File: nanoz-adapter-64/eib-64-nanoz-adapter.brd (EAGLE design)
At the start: 24 x 63.5 mm, 4 parts, among them J1 DF40-REC, J4 SCREW2

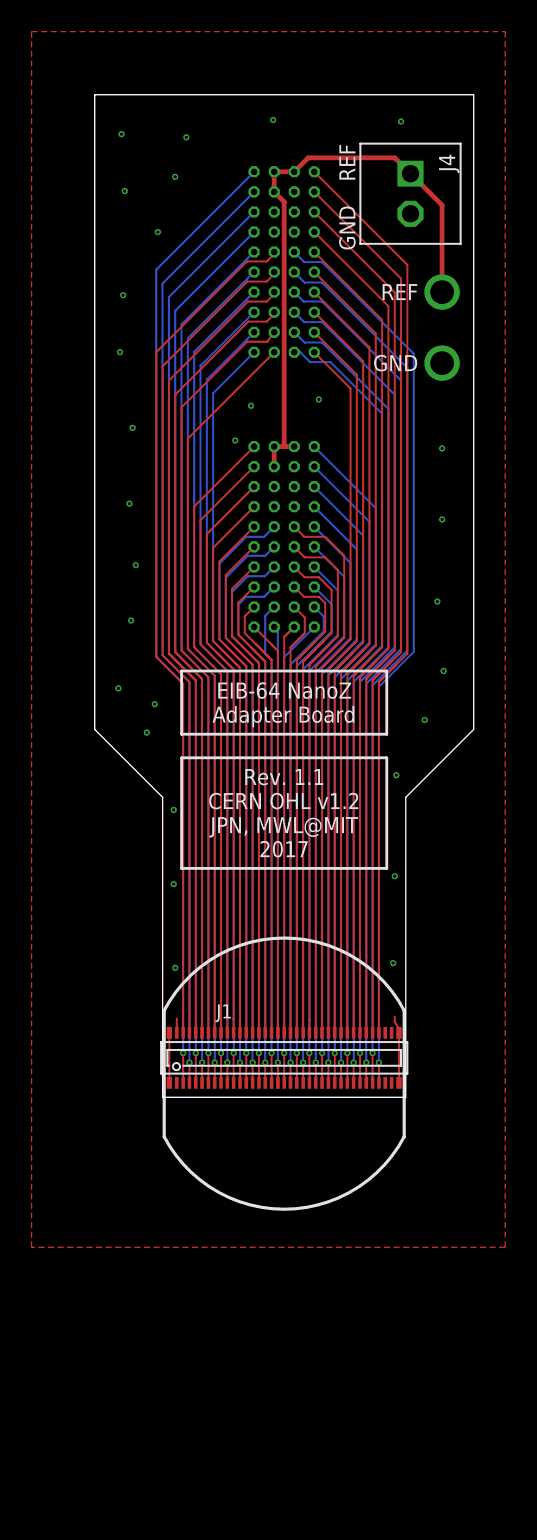
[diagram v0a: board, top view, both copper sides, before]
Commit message: elongated the footprint
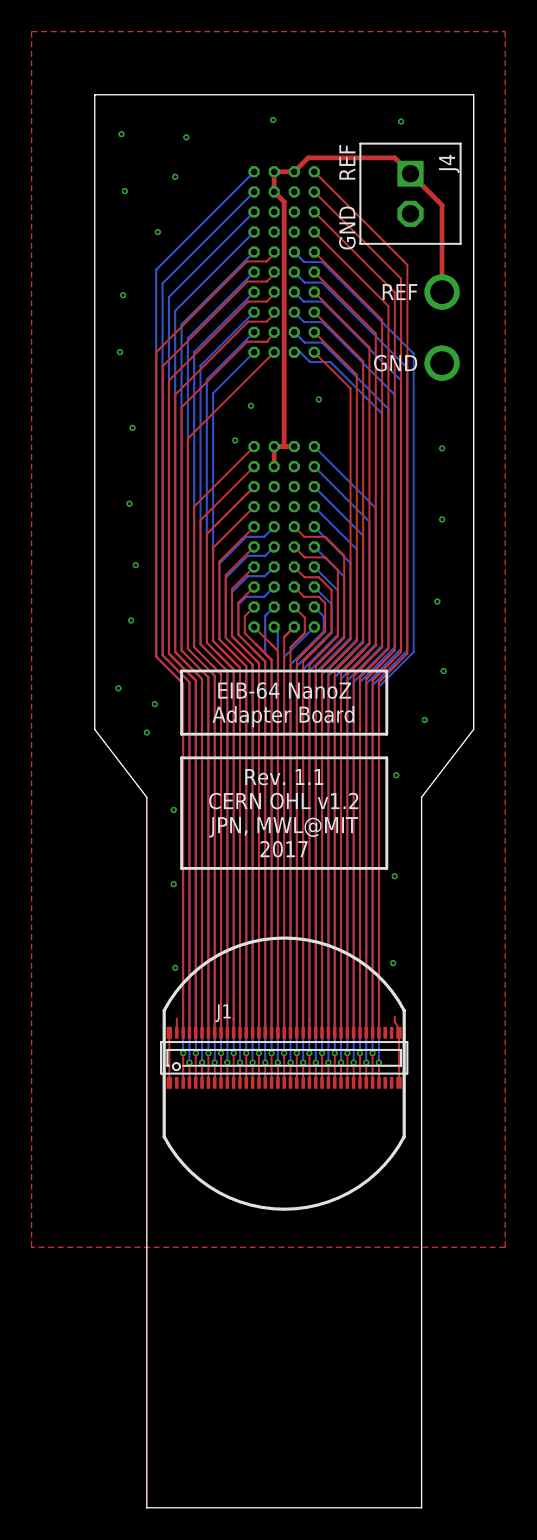
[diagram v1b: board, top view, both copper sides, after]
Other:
- board size 24 x 63.5 mm -> 24 x 89.5 mm
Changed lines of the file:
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@@
 <?xml version="1.0" encoding="utf-8"?>
 <!DOCTYPE eagle SYSTEM "eagle.dtd">
-<eagle version="8.3.2">
+<eagle version="9.5.2">
 <drawing>
 <settings>
@@
 JPN, MWL@MIT
 2017</text>
-<wire x1="7.7" y1="22.5" x2="7.7" y2="41.5" width="0" layer="20"/>
+<wire x1="8.7" y1="-3.5" x2="8.7" y2="41.5" width="0" layer="20"/>
 <wire x1="11.99999375" y1="85.999965625" x2="-11.999996875" y2="85.999975" width="0" layer="20"/>
-<wire x1="-34.999971875" y1="44.99998125" x2="34.999984375" y2="44.99996875" width="0.254" layer="51" style="longdash"/>
-<wire x1="-34.999975" y1="44.999984375" x2="-34.999996875" y2="93.999975" width="0.254" layer="51" style="longdash"/>
-<wire x1="34.999984375" y1="44.999971875" x2="34.999984375" y2="93.999971875" width="0.254" layer="51" style="longdash"/>
 <text x="8.5" y="69" size="1.016" layer="21" font="vector" ratio="18" align="center-right">GND</text>
 <text x="8.5" y="73.5" size="1.016" layer="21" font="vector" ratio="18" align="center-right">REF</text>
@@
 <text x="4" y="79" size="1.016" layer="21" font="vector" ratio="18" rot="R90" align="center-right">GND</text>
 <text x="4" y="80.5" size="1.016" layer="21" font="vector" ratio="18" rot="R270" align="center-right">REF</text>
-<wire x1="-7.7" y1="41.5" x2="-7.7" y2="22.5" width="0" layer="20"/>
+<wire x1="-8.7" y1="41.5" x2="-8.7" y2="-3.5" width="0" layer="20"/>
 <wire x1="-12" y1="45.8" x2="-12" y2="86" width="0" layer="20"/>
 <wire x1="12" y1="45.8" x2="12" y2="86" width="0" layer="20"/>
-<wire x1="-7.7" y1="41.5" x2="-12" y2="45.8" width="0" layer="20"/>
-<wire x1="7.7" y1="41.5" x2="12" y2="45.8" width="0" layer="20"/>
-<wire x1="7.7" y1="22.5" x2="-7.7" y2="22.5" width="0" layer="20"/>
+<wire x1="-8.7" y1="41.5" x2="-12" y2="45.8" width="0" layer="20"/>
+<wire x1="8.7" y1="41.5" x2="12" y2="45.8" width="0" layer="20"/>
+<wire x1="8.7" y1="-3.5" x2="-8.7" y2="-3.5" width="0" layer="20"/>
 </plain>
 <attributes>
@@
 <param name="dpMaxLengthDifference" value="10mm"/>
 <param name="dpGapFactor" value="2.5"/>
-<param name="checkGrid" value="0"/>
 <param name="checkAngle" value="0"/>
 <param name="checkFont" value="1"/>
 <param name="checkRestrict" value="0"/>
+<param name="checkStop" value="0"/>
+<param name="checkValues" value="0"/>
+<param name="checkNames" value="1"/>
+<param name="checkWireStubs" value="1"/>
+<param name="checkPolygonWidth" value="0"/>
 <param name="useDiameter" value="13"/>
 <param name="maxErrors" value="999999"/>
@@
 </signal>
 </signals>
+<mfgpreviewcolors>
+<mfgpreviewcolor name="soldermaskcolor" color="0xC8008000"/>
+<mfgpreviewcolor name="silkscreencolor" color="0xFFFEFEFE"/>
+<mfgpreviewcolor name="backgroundcolor" color="0xFF282828"/>
+<mfgpreviewcolor name="coppercolor" color="0xFFFFBF00"/>
+<mfgpreviewcolor name="substratecolor" color="0xFF786E46"/>
+</mfgpreviewcolors>
 <errors>
 </errors>

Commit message: updated long board to have top and bottom gnd planes
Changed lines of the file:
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@@
 JPN, MWL@MIT
 2017</text>
-<wire x1="8.7" y1="-3.5" x2="8.7" y2="41.5" width="0" layer="20"/>
-<wire x1="11.99999375" y1="85.999965625" x2="-11.999996875" y2="85.999975" width="0" layer="20"/>
+<wire x1="8.7" y1="-3.5" x2="8.7" y2="41.5" width="0.0762" layer="20"/>
+<wire x1="11.99999375" y1="85.999965625" x2="-11.999996875" y2="85.999975" width="0.0762" layer="20"/>
 <text x="8.5" y="69" size="1.016" layer="21" font="vector" ratio="18" align="center-right">GND</text>
 <text x="8.5" y="73.5" size="1.016" layer="21" font="vector" ratio="18" align="center-right">REF</text>
@@
 <text x="4" y="80.5" size="1.016" layer="21" font="vector" ratio="18" rot="R270" align="center-right">REF</text>
 <wire x1="-8.7" y1="41.5" x2="-8.7" y2="-3.5" width="0" layer="20"/>
-<wire x1="-12" y1="45.8" x2="-12" y2="86" width="0" layer="20"/>
-<wire x1="12" y1="45.8" x2="12" y2="86" width="0" layer="20"/>
+<wire x1="-12" y1="45.8" x2="-12" y2="86" width="0.0762" layer="20"/>
+<wire x1="12" y1="45.8" x2="12" y2="86" width="0.0762" layer="20"/>
 <wire x1="-8.7" y1="41.5" x2="-12" y2="45.8" width="0" layer="20"/>
 <wire x1="8.7" y1="41.5" x2="12" y2="45.8" width="0" layer="20"/>
